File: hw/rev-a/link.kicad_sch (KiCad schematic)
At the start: 23 parts, among them J101 TYPE-C-31-M-12, J102 Link cable, U101 USBLC6-2SC6, U102 SN74LVC1T45DBVR, U103 SN74LVC1T45DBVR, U104 SN74LVC1T45DBVR, U105 TPD4E05U06DQAR

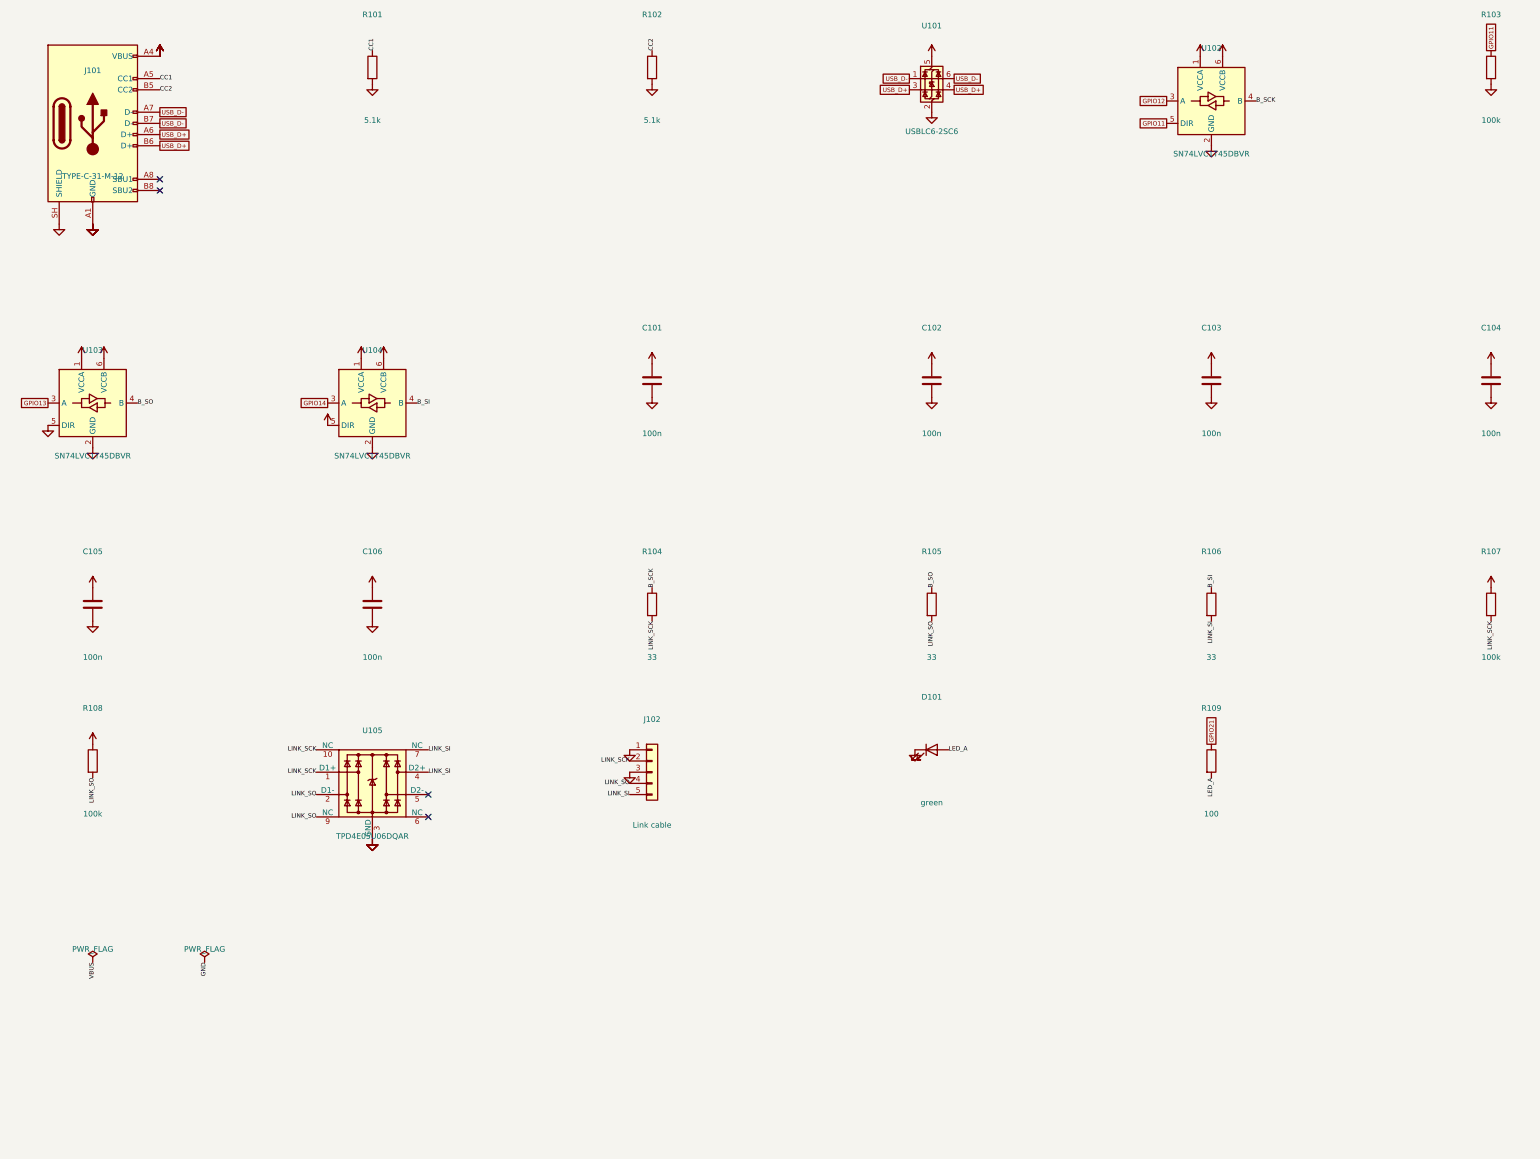
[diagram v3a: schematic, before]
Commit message: PCB rev A: link simulation -> 220R + 100 pF, routing tidy-up, height check, Gerber render, hw README
Co-Authored-By: Claude Opus 5.5 (1M context) <noreply@anthropic.com>
Claude-Session: https://claude.ai/code/session_01MZ3uQJCcn6FcjzVDhZnLJN
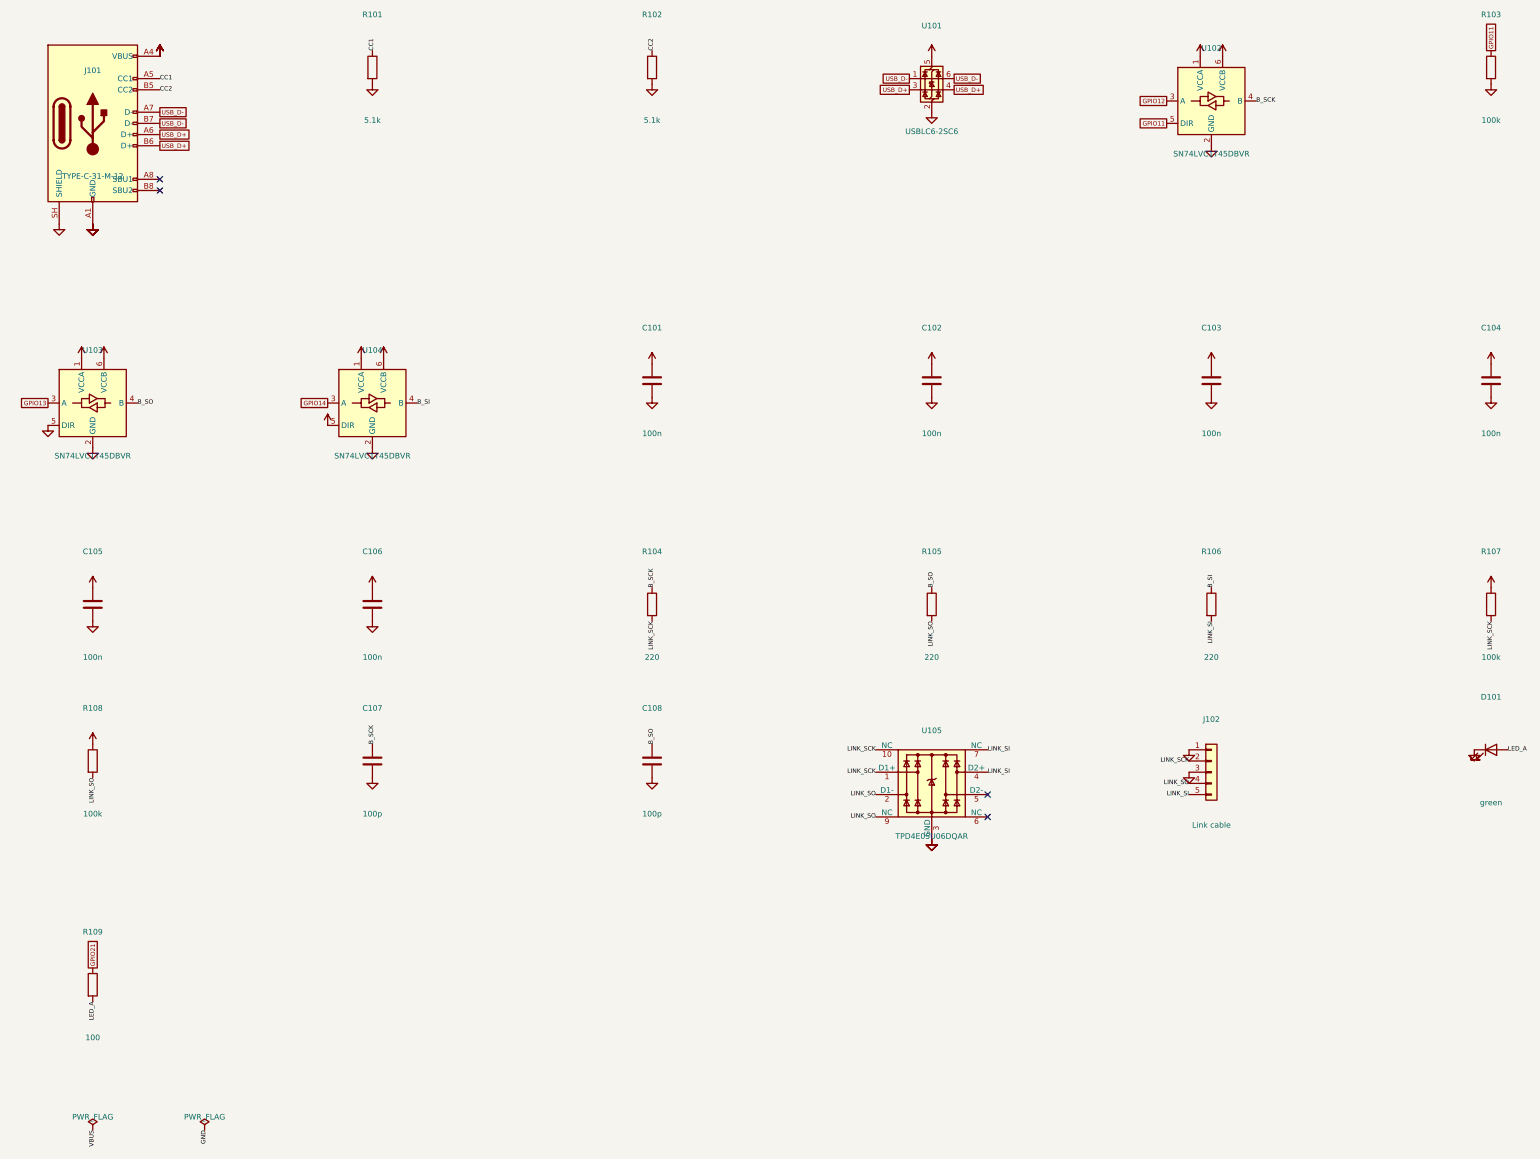
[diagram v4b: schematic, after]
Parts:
- added C107, C108: 100p, Capacitor_SMD:C_0402_1005Metric, symbol Device:C
- R104, R105, R106: value 33 -> 220; LCSC C25105 -> C25091
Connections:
- net B_SCK: now also C107.1
- net B_SO: now also C108.1
- net GND: now also C107.2, C108.2
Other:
- moved on the sheet: D101, J102, R109, U105

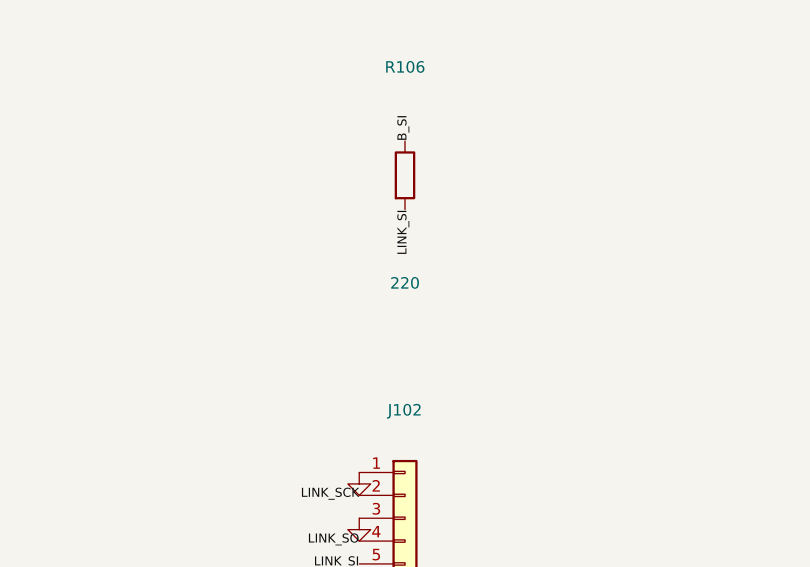
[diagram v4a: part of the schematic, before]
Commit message: PCB rev A: independent review fixes (R106 1k, longer board behind cable holes, USB-C flush, 16 MB flash, docs)
Co-Authored-By: Claude Opus 5.5 (1M context) <noreply@anthropic.com>
Claude-Session: https://claude.ai/code/session_01MZ3uQJCcn6FcjzVDhZnLJN
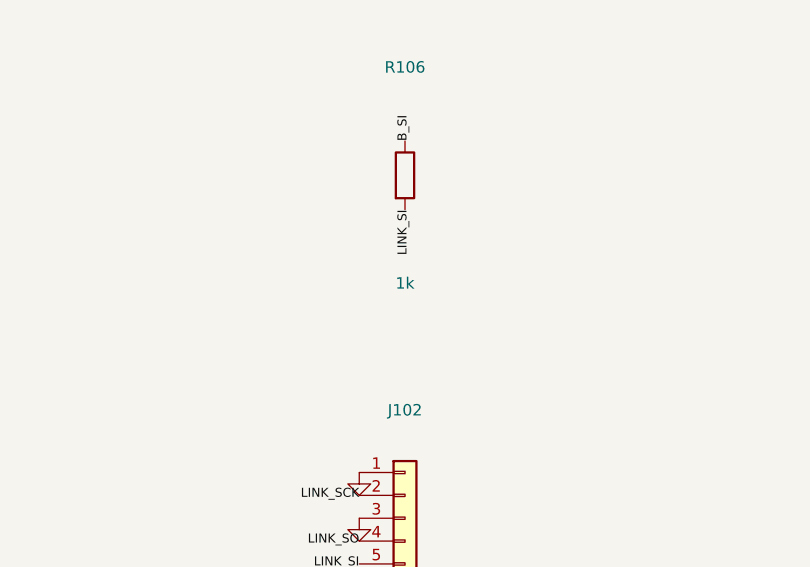
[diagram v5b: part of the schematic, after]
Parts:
- J101: footprint Connector_USB:USB_C_Receptacle_HRO_TYPE-C-31-M-12 -> gb-link-usb:USB_C_Receptacle_HRO_TYPE-C-31-M-12_Flush
- R106: value 220 -> 1k; LCSC C25091 -> C11702
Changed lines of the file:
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@@
 			)
 		)
-		(property "Footprint" "Connector_USB:USB_C_Receptacle_HRO_TYPE-C-31-M-12"
+		(property "Footprint" "gb-link-usb:USB_C_Receptacle_HRO_TYPE-C-31-M-12_Flush"
 			(at 25.4 58.42 0)
 			(effects
@@
 			)
 		)
-		(property "Value" "220"
+		(property "Value" "1k"
 			(at 279.4 179.64 0)
 			(effects
@@
 			)
 		)
-		(property "LCSC" "C25091"
+		(property "LCSC" "C11702"
 			(at 279.4 167.64 0)
 			(effects
